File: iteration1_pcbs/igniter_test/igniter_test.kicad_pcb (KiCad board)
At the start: 2 copper layers, 100 x 65 mm, 42 parts, among them IC1 LM51571QRTERQ1, J1 Conn_01x02, J2 FET_A_P, J3 FET_A_N, J4 FET_B_P, J5 FET_B_N, Q1 STL36DN6F7, Q2 BSS138PW_115, U1 Teensy4.0, U2 MIC4127YME-TR

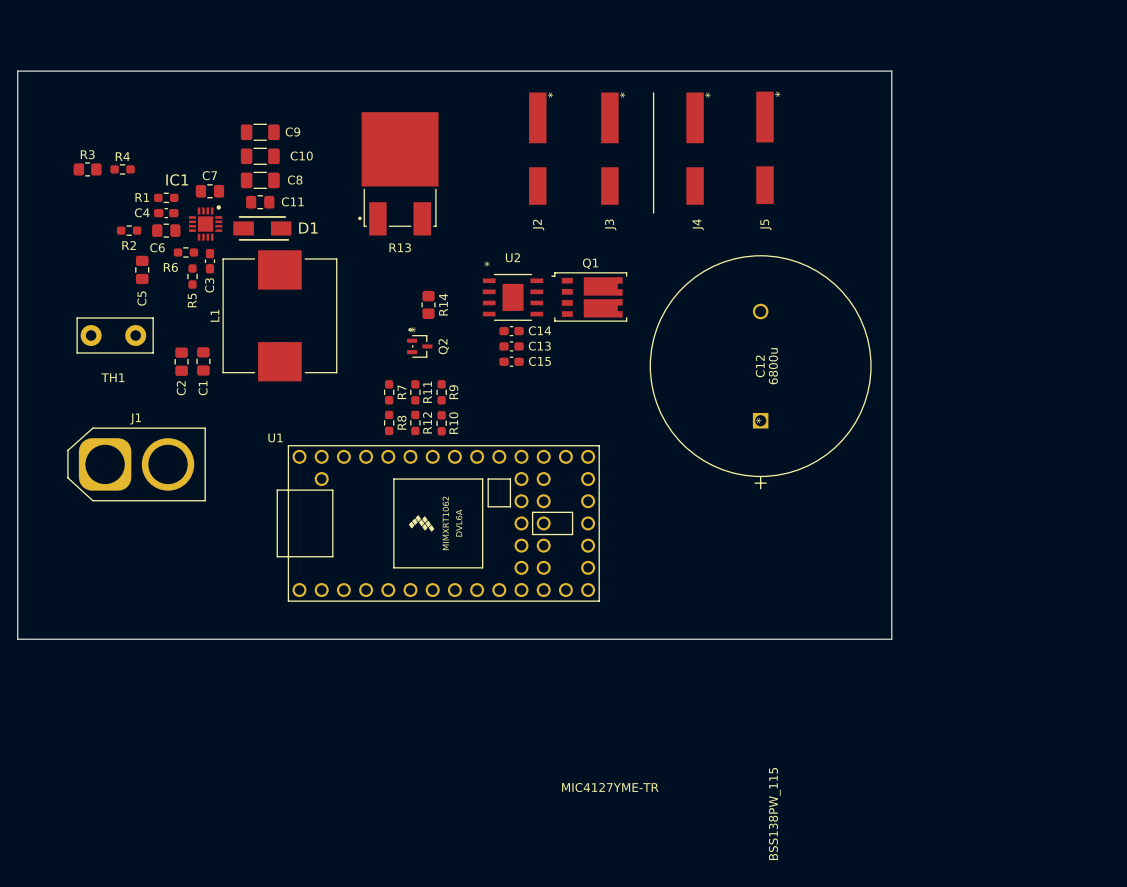
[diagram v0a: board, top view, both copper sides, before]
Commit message: Laying out and wiring the igniter test pcb
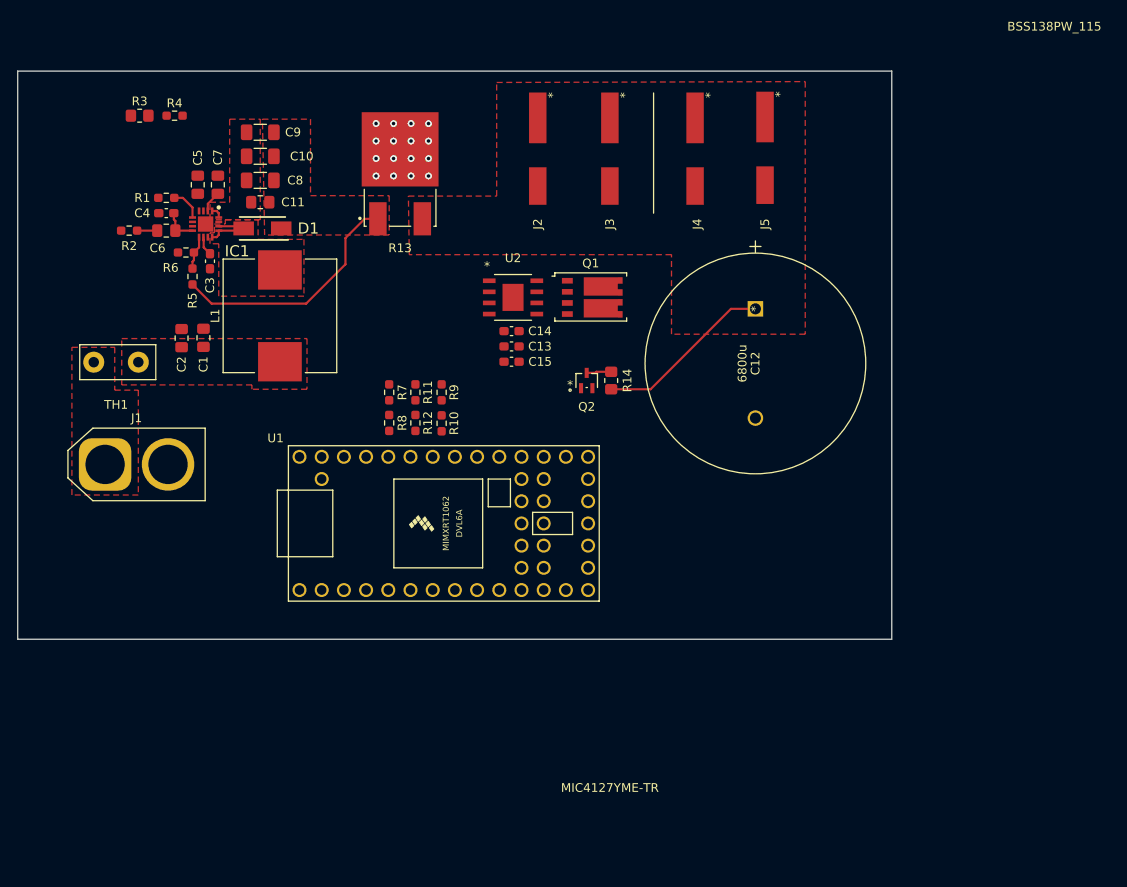
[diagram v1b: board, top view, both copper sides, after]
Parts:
- moved R14 22.6 mm to (162.9, 80.4), turned to 90 degrees
- moved Q2 19.5 mm to (160.1, 80.4), turned to 0 degrees
- moved C12 12.8 mm to (179.4, 72.2), turned to 270 degrees
- moved C5 11.6 mm to (115.6, 58.0)
- moved R3 8.56 mm to (109.0, 50.1)
- moved R4 8.56 mm to (113.0, 50.1)
- moved TH1 3.06 mm to (108.8, 78.3)
- moved C1 2.70 mm to (116.2, 75.5)
- moved C2 2.70 mm to (113.8, 75.5)
- moved C7 1.17 mm to (117.9, 58.0), turned to 270 degrees
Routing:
- net /igniter_actuator/48V: track 0.00 -> 27.9 mm
- net /igniter_actuator/CAP_HIGH: track 0.00 -> 20.3 mm
- net /igniter_actuator/SW: track 0.00 -> 6.56 mm
- net /igniter_actuator/COMP: track 0.00 -> 4.03 mm
- net /igniter_actuator/FB: track 0.00 -> 3.90 mm
- net /igniter_actuator/RT: track 0.00 -> 3.69 mm
- net Net-(Q2-Pad3): track 0.00 -> 2.85 mm
- net Net-(C7-Pad2): track 0.00 -> 2.44 mm
- net Net-(C6-Pad2): track 0.00 -> 2.30 mm
- net /igniter_actuator/SS: track 0.00 -> 2.20 mm
- net GND: track 0.00 -> 1.35 mm, vias 0 -> 16
- added copper zone on F.Cu, net /VBAT
- added copper zone on F.Cu, net /igniter_actuator/48V
- added copper zone on F.Cu, net /igniter_actuator/CAP_HIGH
- added copper zone on F.Cu, net /igniter_actuator/SW
- added copper zone on F.Cu, net GND
- added copper zone on In1.Cu, net GND
- added copper zone on In2.Cu, net GND
- added copper zone on F.Cu, net VCC
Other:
- copper layers 2 -> 4

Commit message: igniter test tracks
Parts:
- added R15: 37.4k, Resistor_SMD:R_0603_1608Metric_Pad0.98x0.95mm_HandSolder, F.Cu at (112.3, 69.3)
- C13, C14, C15, Q1, Q2, R14, U2: moved to B.Cu
- J1: value Conn_01x02 -> XT60
- R3: value 665k -> 274k; footprint Resistor_SMD:R_0805_2012Metric_Pad1.20x1.40mm_HandSolder -> Resistor_SMD:R_0603_1608Metric_Pad0.98x0.95mm_HandSolder
- R4: value 200k -> 95.3k
- moved U2 18.2 mm to (169.8, 69.4), turned to 90 degrees
- moved J2 17.8 mm to (172.3, 55.0)
- moved J3 17.8 mm to (180.6, 55.0)
- moved J4 17.2 mm to (155.3, 55.0)
- moved J5 17.2 mm to (163.3, 55.0)
- moved C14 15.3 mm to (165.9, 69.6), turned to 270 degrees
- moved C13 14.5 mm to (164.2, 69.6), turned to 270 degrees
- moved C12 14.0 mm to (177.7, 86.1), turned to 180 degrees
- moved C15 14.0 mm to (162.4, 69.6), turned to 270 degrees
- moved Q1 13.9 mm to (169.8, 60.5), turned to 90 degrees
- moved Q2 10.6 mm to (167.8, 87.7)
- moved R14 10.6 mm to (170.6, 87.7), turned to 270 degrees
- moved U1 6.35 mm to (137.5, 97.9)
- moved R3 5.04 mm to (110.5, 54.9)
- moved R4 3.97 mm to (113.7, 54.0), turned to 90 degrees
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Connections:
- IC1 pad 11: GND -> /igniter_actuator/MODE
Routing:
- net GND: track 1.35 -> 96.0 mm, vias 16 -> 43
- net VCC: track 0.00 -> 83.7 mm, vias 0 -> 3
- net /PYRO_A: track 0.00 -> 65.1 mm
- net /igniter_actuator/FET_A: track 0.00 -> 64.4 mm, vias 0 -> 2
- net /PYRO_B: track 0.00 -> 58.8 mm
- net /igniter_actuator/FET_B: track 0.00 -> 50.5 mm, vias 0 -> 2
- net /CAP_DCHG: track 0.00 -> 42.7 mm
- net /igniter_actuator/CAP_HIGH: track 20.3 -> 51.9 mm
- net /PY_SENSE_A: track 0.00 -> 15.4 mm
- net /igniter_actuator/EN: track 0.00 -> 12.4 mm
- net /PY_SENSE_B: track 0.00 -> 11.0 mm
- net /CAP_SENSE: track 0.00 -> 10.5 mm
- net /igniter_actuator/MODE: track 0.00 -> 8.09 mm, vias 0 -> 2
- net /igniter_actuator/OUTB: track 0.00 -> 3.50 mm
- net /igniter_actuator/OUTA: track 0.00 -> 3.49 mm
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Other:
- net class Thicc added: clearance 0.4, trace_width 0.75, via_dia 1, via_drill 0.5

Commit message: Adding most of the changes, almost don
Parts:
- added H1: MountingHole_Pad, MountingHole:MountingHole_3.2mm_M3_Pad_Via, F.Cu at (100.0, 50.0)
- added H2: MountingHole_Pad, MountingHole:MountingHole_3.2mm_M3_Pad_Via, F.Cu at (190.0, 50.0)
- added H3: MountingHole_Pad, MountingHole:MountingHole_3.2mm_M3_Pad_Via, F.Cu at (100.0, 105.0)
- added H4: MountingHole_Pad, MountingHole:MountingHole_3.2mm_M3_Pad_Via, F.Cu at (190.0, 105.0)
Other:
- outline, holes or cut-outs redrawn
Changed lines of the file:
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@@
   (general
     (thickness 1.6)
-    (drawings 5)
+    (drawings 9)
     (tracks 236)
     (zones 0)
-    (modules 43)
+    (modules 47)
     (nets 68)
   )
@@
       (effects (font (size 1 1) (thickness 0.15)))
     )
-    (fp_text user %R (at 0 0) (layer F.Fab)
-      (effects (font (size 0.4 0.4) (thickness 0.06)))
-    )
     (fp_line (start -0.8 0.4125) (end -0.8 -0.4125) (layer F.Fab) (width 0.1))
     (fp_line (start -0.8 -0.4125) (end 0.8 -0.4125) (layer F.Fab) (width 0.1))
@@
     (fp_line (start 1.65 -0.73) (end 1.65 0.73) (layer F.CrtYd) (width 0.05))
     (fp_line (start 1.65 0.73) (end -1.65 0.73) (layer F.CrtYd) (width 0.05))
+    (fp_text user %R (at 0 0) (layer F.Fab)
+      (effects (font (size 0.4 0.4) (thickness 0.06)))
+    )
     (pad 2 smd roundrect (at 0.9125 0) (size 0.975 0.95) (layers F.Cu F.Paste F.Mask) (roundrect_rratio 0.25)
       (net 65 /igniter_actuator/EN))
@@
   (module iteration1:UVR1H682MRD6 (layer F.Cu)
     (at 177.7 86.1 180)
+    (zone_connect 2)
     (fp_text reference C12 (at 6.2484 0) (layer F.SilkS)
       (effects (font (size 1 1) (thickness 0.15)))
@@
     )
     (pad 1 thru_hole rect (at 0 0 180) (size 1.778 1.778) (drill 1.27) (layers *.Cu *.Mask)
-      (net 8 /igniter_actuator/CAP_HIGH))
+      (net 8 /igniter_actuator/CAP_HIGH) (zone_connect 2))
     (pad 2 thru_hole circle (at 12.4968 0 180) (size 1.778 1.778) (drill 1.27) (layers *.Cu *.Mask)
-      (net 2 GND))
+      (net 2 GND) (zone_connect 2))
   )
   (module Capacitor_SMD:C_0603_1608Metric_Pad1.08x0.95mm_HandSolder (layer B.Cu)
@@
     )
   )
-  (gr_line (start 95 110) (end 95 45) (layer Edge.Cuts) (width 0.05))
-  (gr_line (start 195 110) (end 95 110) (layer Edge.Cuts) (width 0.05))
-  (gr_line (start 195 45) (end 195 110) (layer Edge.Cuts) (width 0.05))
-  (gr_line (start 95 45) (end 195 45) (layer Edge.Cuts) (width 0.05))
+  (module MountingHole:MountingHole_3.2mm_M3_Pad_Via (layer F.Cu)
+    (at 100 50)
+    (descr "Mounting Hole 3.2mm, M3")
+    (tags "mounting hole 3.2mm m3")
+    (attr virtual)
+    (fp_text reference H1 (at 0 -4.2) (layer F.SilkS)
+      (effects (font (size 1 1) (thickness 0.15)))
+    )
+    (fp_text value MountingHole_Pad (at 0 4.2) (layer F.Fab)
+      (effects (font (size 1 1) (thickness 0.15)))
+    )
+    (fp_text user %R (at 0.3 0) (layer F.Fab)
+      (effects (font (size 1 1) (thickness 0.15)))
+    )
+    (fp_circle (center 0 0) (end 3.2 0) (layer Cmts.User) (width 0.15))
+    (fp_circle (center 0 0) (end 3.45 0) (layer F.CrtYd) (width 0.05))
+    (pad 1 thru_hole circle (at 1.697056 -1.697056) (size 0.8 0.8) (drill 0.5) (layers *.Cu *.Mask)
+      (net 2 GND))
+    (pad 1 thru_hole circle (at 0 -2.4) (size 0.8 0.8) (drill 0.5) (layers *.Cu *.Mask)
+      (net 2 GND))
+    (pad 1 thru_hole circle (at -1.697056 -1.697056) (size 0.8 0.8) (drill 0.5) (layers *.Cu *.Mask)
+      (net 2 GND))
+    (pad 1 thru_hole circle (at -2.4 0) (size 0.8 0.8) (drill 0.5) (layers *.Cu *.Mask)
+      (net 2 GND))
+    (pad 1 thru_hole circle (at -1.697056 1.697056) (size 0.8 0.8) (drill 0.5) (layers *.Cu *.Mask)
+      (net 2 GND))
+    (pad 1 thru_hole circle (at 0 2.4) (size 0.8 0.8) (drill 0.5) (layers *.Cu *.Mask)
+      (net 2 GND))
+    (pad 1 thru_hole circle (at 1.697056 1.697056) (size 0.8 0.8) (drill 0.5) (layers *.Cu *.Mask)
+      (net 2 GND))
+    (pad 1 thru_hole circle (at 2.4 0) (size 0.8 0.8) (drill 0.5) (layers *.Cu *.Mask)
+      (net 2 GND))
+    (pad 1 thru_hole circle (at 0 0) (size 6.4 6.4) (drill 3.2) (layers *.Cu *.Mask)
+      (net 2 GND))
+  )
+  (module MountingHole:MountingHole_3.2mm_M3_Pad_Via (layer F.Cu)
+    (at 190 50)
+    (descr "Mounting Hole 3.2mm, M3")
+    (tags "mounting hole 3.2mm m3")
+    (attr virtual)
+    (fp_text reference H2 (at 0 -4.2) (layer F.SilkS)
+      (effects (font (size 1 1) (thickness 0.15)))
+    )
+    (fp_text value MountingHole_Pad (at 0 4.2) (layer F.Fab)
+      (effects (font (size 1 1) (thickness 0.15)))
+    )
+    (fp_circle (center 0 0) (end 3.45 0) (layer F.CrtYd) (width 0.05))
+    (fp_circle (center 0 0) (end 3.2 0) (layer Cmts.User) (width 0.15))
+    (fp_text user %R (at 0.3 0) (layer F.Fab)
+      (effects (font (size 1 1) (thickness 0.15)))
+    )
+    (pad 1 thru_hole circle (at 0 0) (size 6.4 6.4) (drill 3.2) (layers *.Cu *.Mask)
+      (net 2 GND))
+    (pad 1 thru_hole circle (at 2.4 0) (size 0.8 0.8) (drill 0.5) (layers *.Cu *.Mask)
+      (net 2 GND))
+    (pad 1 thru_hole circle (at 1.697056 1.697056) (size 0.8 0.8) (drill 0.5) (layers *.Cu *.Mask)
+      (net 2 GND))
+    (pad 1 thru_hole circle (at 0 2.4) (size 0.8 0.8) (drill 0.5) (layers *.Cu *.Mask)
+      (net 2 GND))
+    (pad 1 thru_hole circle (at -1.697056 1.697056) (size 0.8 0.8) (drill 0.5) (layers *.Cu *.Mask)
+      (net 2 GND))
+    (pad 1 thru_hole circle (at -2.4 0) (size 0.8 0.8) (drill 0.5) (layers *.Cu *.Mask)
+      (net 2 GND))
+    (pad 1 thru_hole circle (at -1.697056 -1.697056) (size 0.8 0.8) (drill 0.5) (layers *.Cu *.Mask)
+      (net 2 GND))
+    (pad 1 thru_hole circle (at 0 -2.4) (size 0.8 0.8) (drill 0.5) (layers *.Cu *.Mask)
+      (net 2 GND))
+    (pad 1 thru_hole circle (at 1.697056 -1.697056) (size 0.8 0.8) (drill 0.5) (layers *.Cu *.Mask)
+      (net 2 GND))
+  )
+  (module MountingHole:MountingHole_3.2mm_M3_Pad_Via (layer F.Cu)
+    (at 100 105)
+    (descr "Mounting Hole 3.2mm, M3")
+    (tags "mounting hole 3.2mm m3")
+    (attr virtual)
+    (fp_text reference H3 (at 0 -4.2) (layer F.SilkS)
+      (effects (font (size 1 1) (thickness 0.15)))
+    )
+    (fp_text value MountingHole_Pad (at 0 4.2) (layer F.Fab)
+      (effects (font (size 1 1) (thickness 0.15)))
+    )
+    (fp_text user %R (at 0.3 0) (layer F.Fab)
+      (effects (font (size 1 1) (thickness 0.15)))
+    )
+    (fp_circle (center 0 0) (end 3.2 0) (layer Cmts.User) (width 0.15))
+    (fp_circle (center 0 0) (end 3.45 0) (layer F.CrtYd) (width 0.05))
+    (pad 1 thru_hole circle (at 1.697056 -1.697056) (size 0.8 0.8) (drill 0.5) (layers *.Cu *.Mask)
+      (net 2 GND))
+    (pad 1 thru_hole circle (at 0 -2.4) (size 0.8 0.8) (drill 0.5) (layers *.Cu *.Mask)
+      (net 2 GND))
+    (pad 1 thru_hole circle (at -1.697056 -1.697056) (size 0.8 0.8) (drill 0.5) (layers *.Cu *.Mask)
+      (net 2 GND))
+    (pad 1 thru_hole circle (at -2.4 0) (size 0.8 0.8) (drill 0.5) (layers *.Cu *.Mask)
+      (net 2 GND))
+    (pad 1 thru_hole circle (at -1.697056 1.697056) (size 0.8 0.8) (drill 0.5) (layers *.Cu *.Mask)
+      (net 2 GND))
+    (pad 1 thru_hole circle (at 0 2.4) (size 0.8 0.8) (drill 0.5) (layers *.Cu *.Mask)
+      (net 2 GND))
+    (pad 1 thru_hole circle (at 1.697056 1.697056) (size 0.8 0.8) (drill 0.5) (layers *.Cu *.Mask)
+      (net 2 GND))
+    (pad 1 thru_hole circle (at 2.4 0) (size 0.8 0.8) (drill 0.5) (layers *.Cu *.Mask)
+      (net 2 GND))
+    (pad 1 thru_hole circle (at 0 0) (size 6.4 6.4) (drill 3.2) (layers *.Cu *.Mask)
+      (net 2 GND))
+  )
+  (module MountingHole:MountingHole_3.2mm_M3_Pad_Via (layer F.Cu)
+    (at 190 105)
+    (descr "Mounting Hole 3.2mm, M3")
+    (tags "mounting hole 3.2mm m3")
+    (attr virtual)
+    (fp_text reference H4 (at 0 -4.2) (layer F.SilkS)
+      (effects (font (size 1 1) (thickness 0.15)))
+    )
+    (fp_text value MountingHole_Pad (at 0 4.2) (layer F.Fab)
+      (effects (font (size 1 1) (thickness 0.15)))
+    )
+    (fp_circle (center 0 0) (end 3.45 0) (layer F.CrtYd) (width 0.05))
+    (fp_circle (center 0 0) (end 3.2 0) (layer Cmts.User) (width 0.15))
+    (fp_text user %R (at 0.3 0) (layer F.Fab)
+      (effects (font (size 1 1) (thickness 0.15)))
+    )
+    (pad 1 thru_hole circle (at 0 0) (size 6.4 6.4) (drill 3.2) (layers *.Cu *.Mask)
+      (net 2 GND))
+    (pad 1 thru_hole circle (at 2.4 0) (size 0.8 0.8) (drill 0.5) (layers *.Cu *.Mask)
+      (net 2 GND))
+    (pad 1 thru_hole circle (at 1.697056 1.697056) (size 0.8 0.8) (drill 0.5) (layers *.Cu *.Mask)
+      (net 2 GND))
+    (pad 1 thru_hole circle (at 0 2.4) (size 0.8 0.8) (drill 0.5) (layers *.Cu *.Mask)
+      (net 2 GND))
+    (pad 1 thru_hole circle (at -1.697056 1.697056) (size 0.8 0.8) (drill 0.5) (layers *.Cu *.Mask)
+      (net 2 GND))
+    (pad 1 thru_hole circle (at -2.4 0) (size 0.8 0.8) (drill 0.5) (layers *.Cu *.Mask)
+      (net 2 GND))
+    (pad 1 thru_hole circle (at -1.697056 -1.697056) (size 0.8 0.8) (drill 0.5) (layers *.Cu *.Mask)
+      (net 2 GND))
+    (pad 1 thru_hole circle (at 0 -2.4) (size 0.8 0.8) (drill 0.5) (layers *.Cu *.Mask)
+      (net 2 GND))
+    (pad 1 thru_hole circle (at 1.697056 -1.697056) (size 0.8 0.8) (drill 0.5) (layers *.Cu *.Mask)
+      (net 2 GND))
+  )
+  (gr_arc (start 190 105) (end 190 110) (angle -90) (layer Edge.Cuts) (width 0.05))
+  (gr_arc (start 100 105) (end 95 105) (angle -90) (layer Edge.Cuts) (width 0.05))
+  (gr_arc (start 100 50) (end 100 45) (angle -90) (layer Edge.Cuts) (width 0.05))
+  (gr_arc (start 190 50) (end 195 50) (angle -90) (layer Edge.Cuts) (width 0.05))
+  (gr_line (start 95 105) (end 95 50) (layer Edge.Cuts) (width 0.05))
+  (gr_line (start 190 110) (end 100 110) (layer Edge.Cuts) (width 0.05))
+  (gr_line (start 195 50) (end 195 105) (layer Edge.Cuts) (width 0.05))
+  (gr_line (start 100 45) (end 190 45) (layer Edge.Cuts) (width 0.05))
   (gr_line (start 167.75 47.5) (end 167.75 61.25) (layer F.SilkS) (width 0.12))
   (via (at 116.5 62.5) (size 0.8) (drill 0.4) (layers F.Cu B.Cu) (net 2))
